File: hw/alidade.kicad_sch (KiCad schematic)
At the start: 0 parts

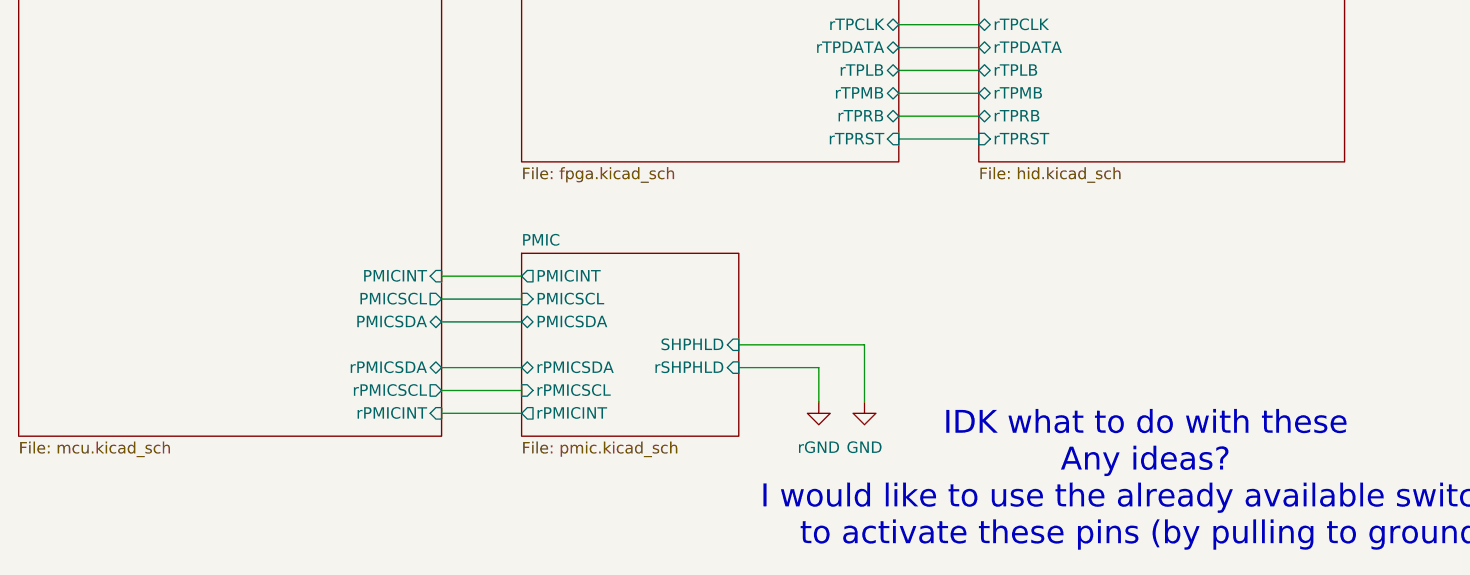
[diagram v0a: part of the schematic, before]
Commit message: Add license and organize repo
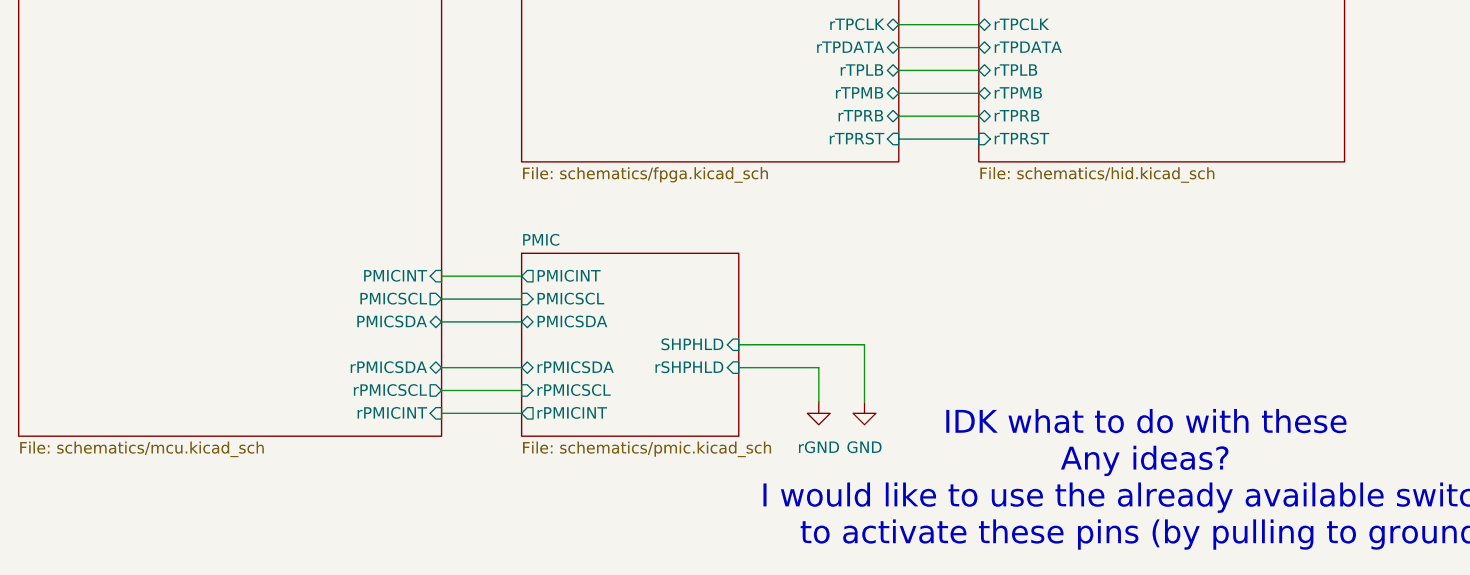
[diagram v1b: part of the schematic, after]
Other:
- sheet FPGA: file fpga.kicad_sch -> schematics/fpga.kicad_sch
- sheet HID: file hid.kicad_sch -> schematics/hid.kicad_sch
- sheet MCU: file mcu.kicad_sch -> schematics/mcu.kicad_sch
- sheet PMIC: file pmic.kicad_sch -> schematics/pmic.kicad_sch
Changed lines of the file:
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@@
 			)
 		)
-		(property "Sheetfile" "pmic.kicad_sch"
+		(property "Sheetfile" "schematics/pmic.kicad_sch"
 			(at 182.88 197.4346 0)
 			(effects
@@
 			)
 		)
-		(property "Sheetfile" "hid.kicad_sch"
+		(property "Sheetfile" "schematics/hid.kicad_sch"
 			(at 233.68 166.9546 0)
 			(effects
@@
 			)
 		)
-		(property "Sheetfile" "mcu.kicad_sch"
+		(property "Sheetfile" "schematics/mcu.kicad_sch"
 			(at 127 197.4346 0)
 			(effects
@@
 			)
 		)
-		(property "Sheetfile" "fpga.kicad_sch"
+		(property "Sheetfile" "schematics/fpga.kicad_sch"
 			(at 182.88 166.9546 0)
 			(effects

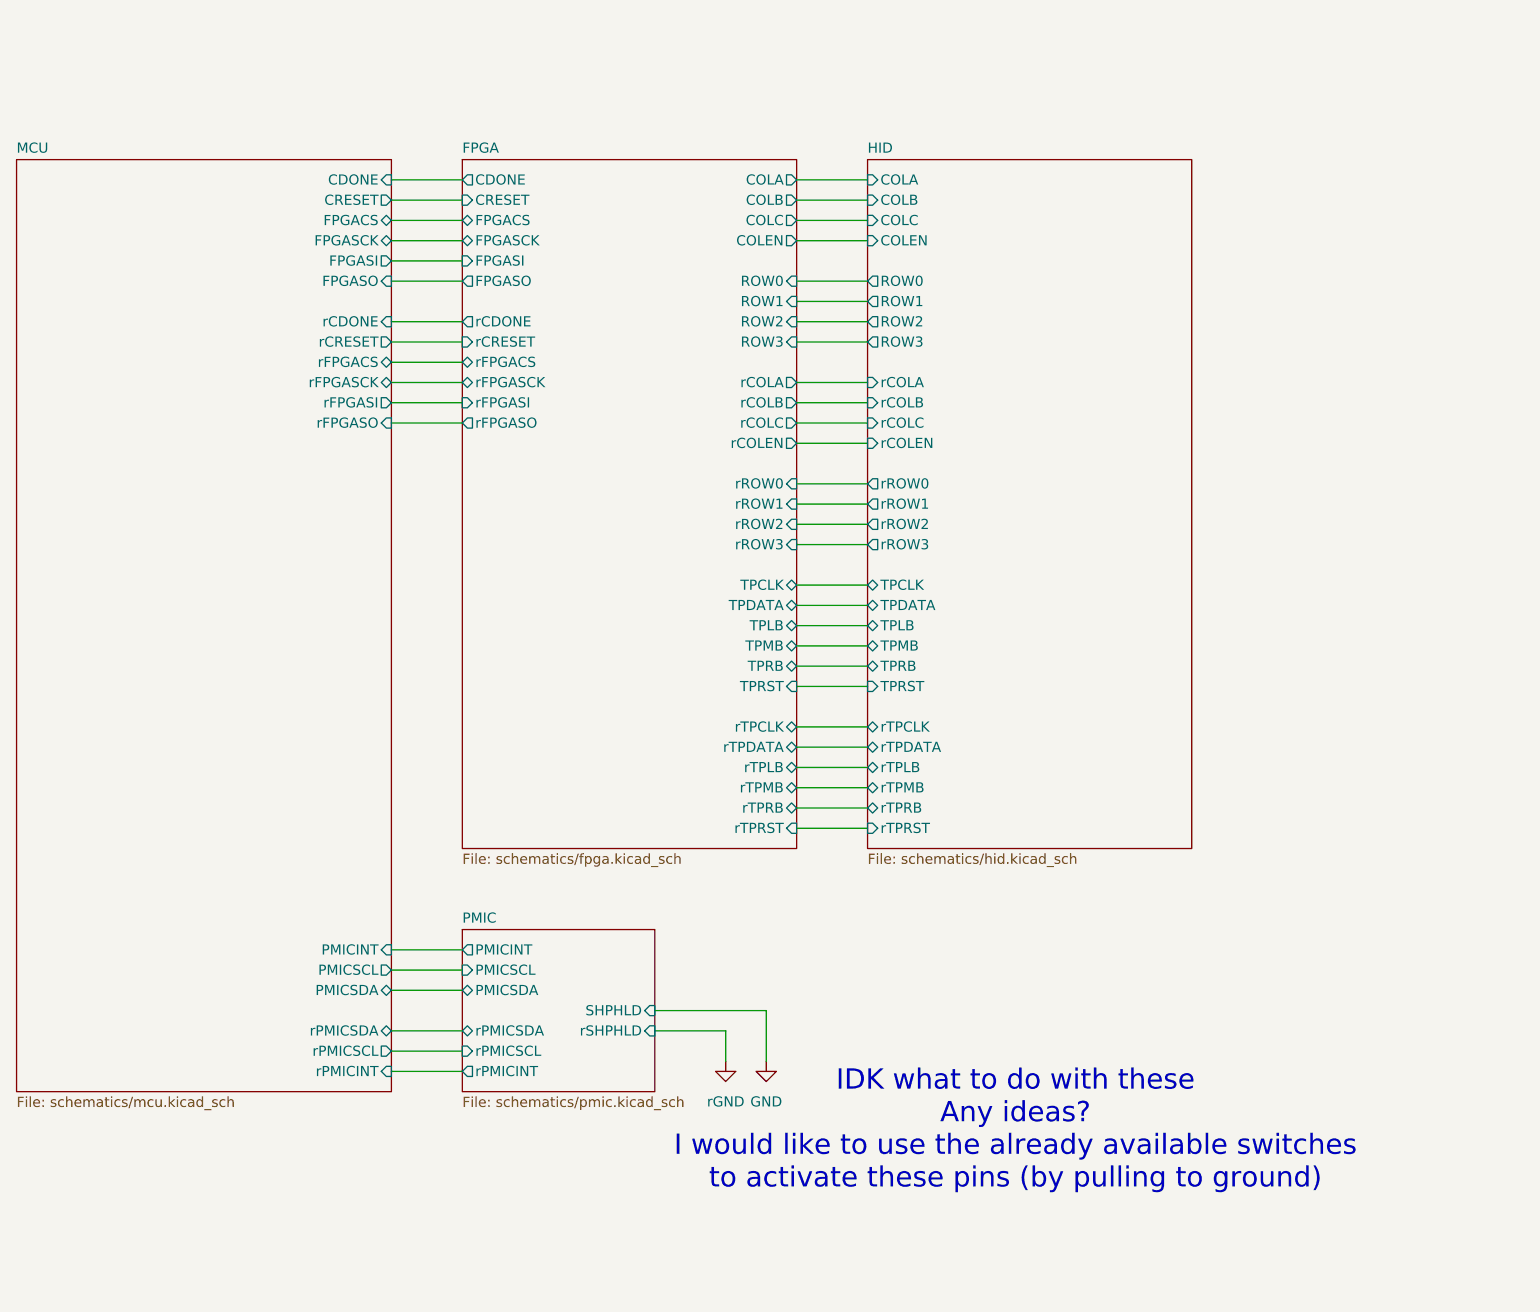
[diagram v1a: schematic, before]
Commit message: Remove SN74LVC138A as we now have enough pins on the UP
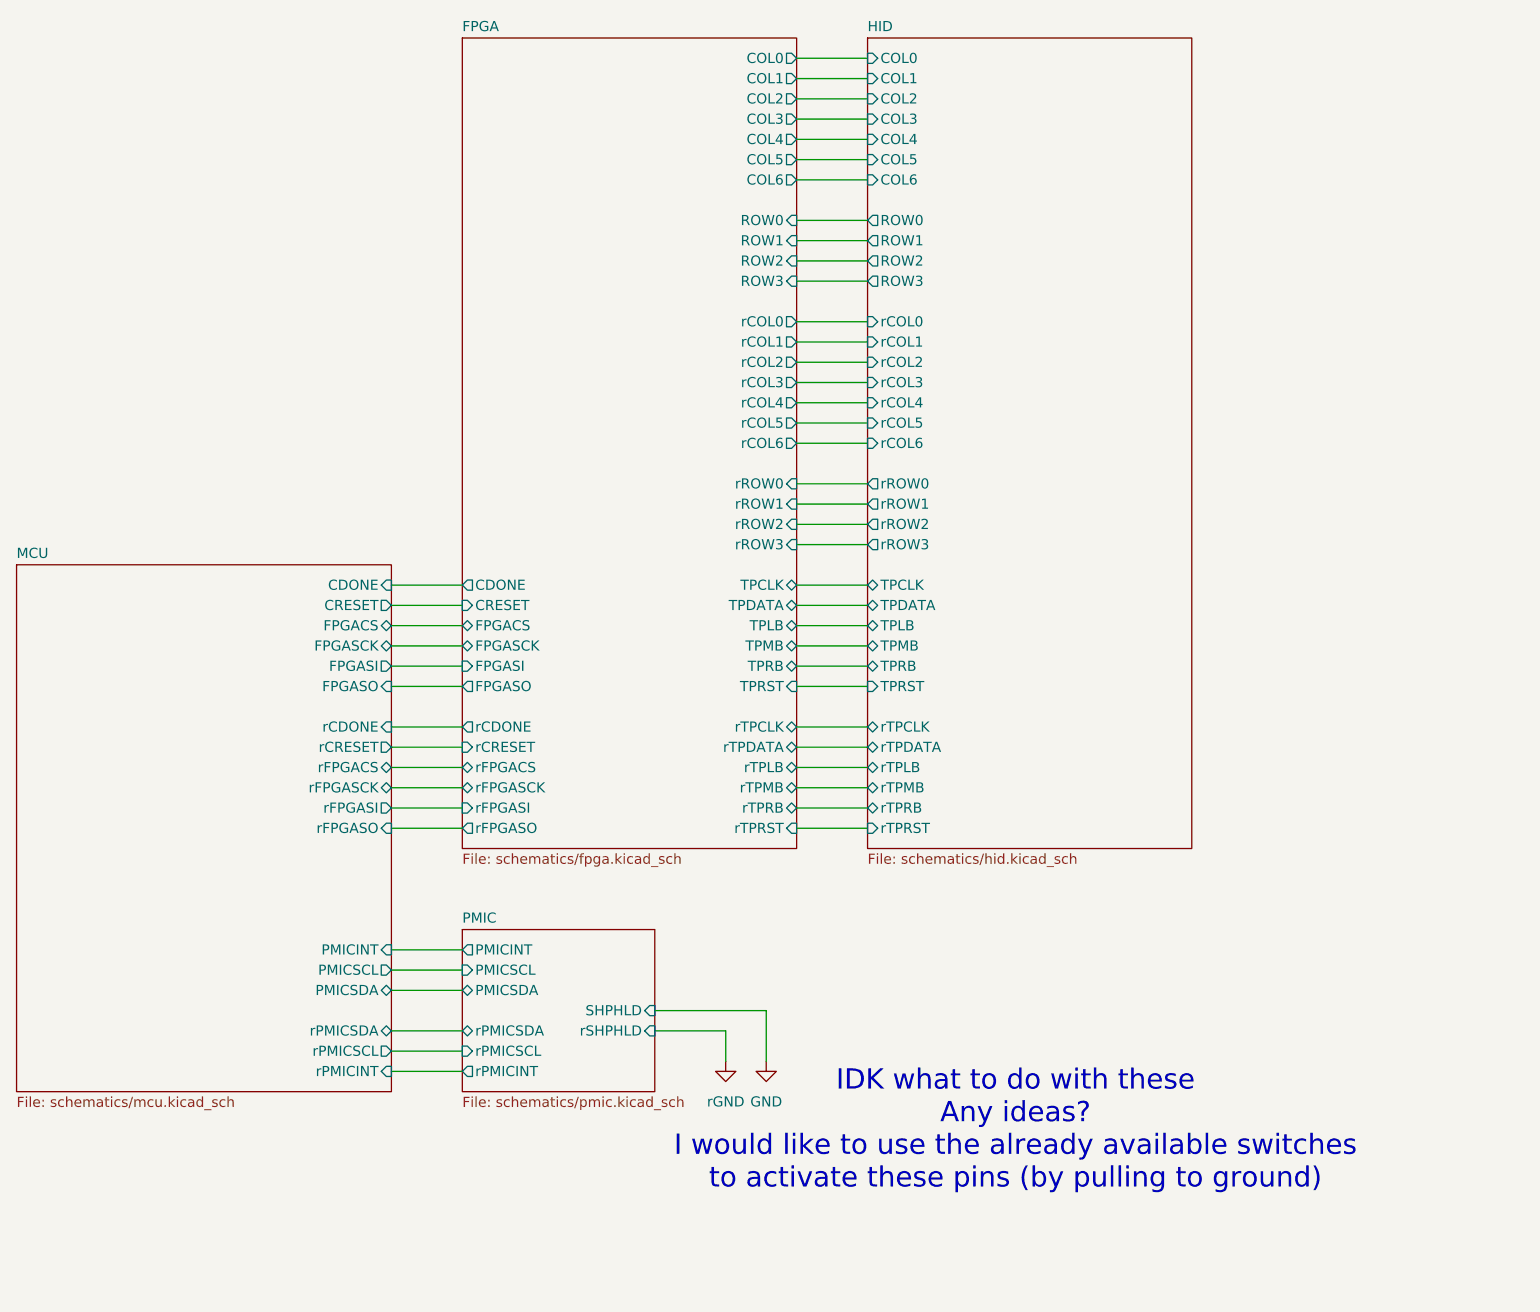
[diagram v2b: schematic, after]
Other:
- sheet FPGA ports: added COL0, COL1, COL2, COL3, COL4, COL5, COL6, rCOL0, rCOL1, rCOL2, rCOL3, rCOL4, rCOL5, rCOL6; removed COLA, COLB, COLC, COLEN, rCOLA, rCOLB, rCOLC, rCOLEN
- sheet HID ports: added COL0, COL1, COL2, COL3, COL4, COL5, COL6, rCOL0, rCOL1, rCOL2, rCOL3, rCOL4, rCOL5, rCOL6; removed COLA, COLB, COLC, COLEN, rCOLA, rCOLB, rCOLC, rCOLEN

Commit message: Remove FPGA, no longer needed
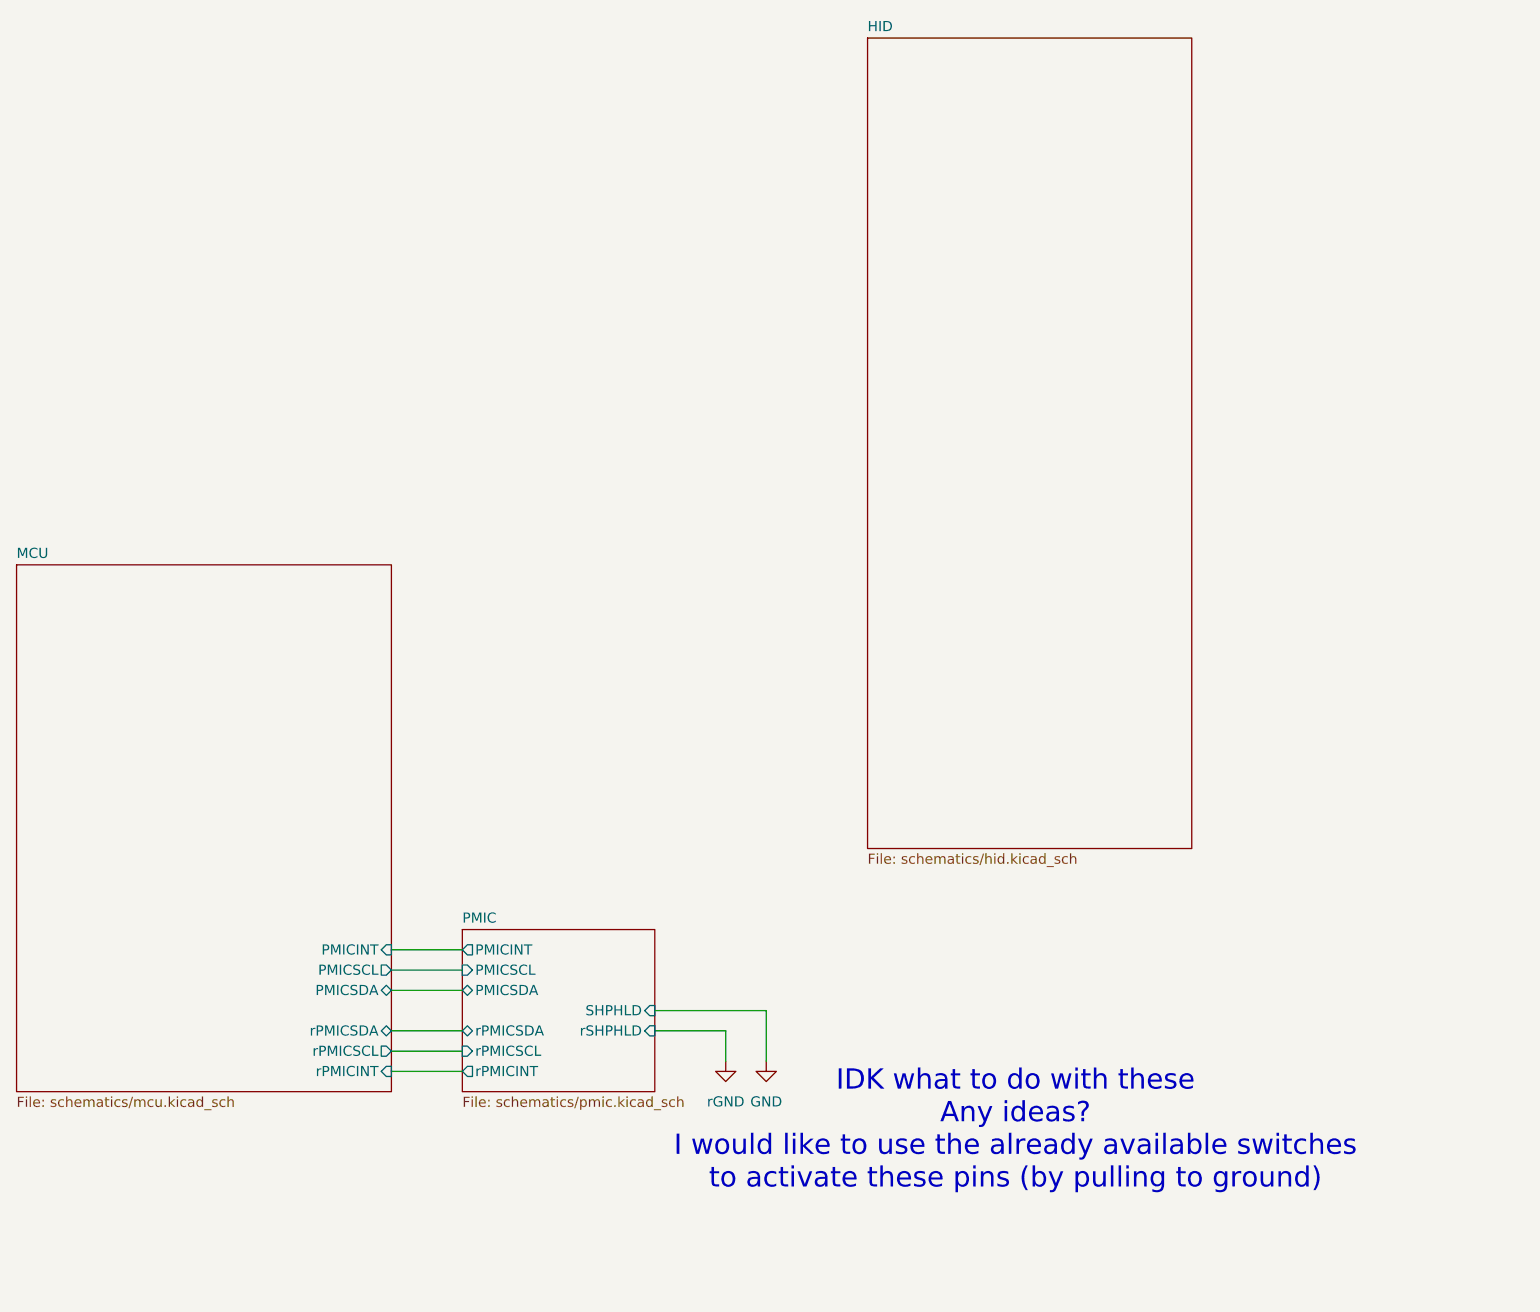
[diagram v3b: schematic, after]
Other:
- removed sheet FPGA
- sheet HID ports: added none; removed COL0, COL1, COL2, COL3, COL4, COL5, COL6, ROW0, ROW1, ROW2, ROW3, TPCLK, TPDATA, TPLB, TPMB, TPRB, TPRST, rCOL0, rCOL1, rCOL2, rCOL3, rCOL4, rCOL5, rCOL6, rROW0, rROW1, rROW2, rROW3, rTPCLK, rTPDATA, rTPLB, rTPMB, rTPRB, rTPRST
- sheet MCU ports: added none; removed CDONE, CRESET, FPGACS, FPGASCK, FPGASI, FPGASO, rCDONE, rCRESET, rFPGACS, rFPGASCK, rFPGASI, rFPGASO

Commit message: Update symbol, use ads122S for bridge measurement
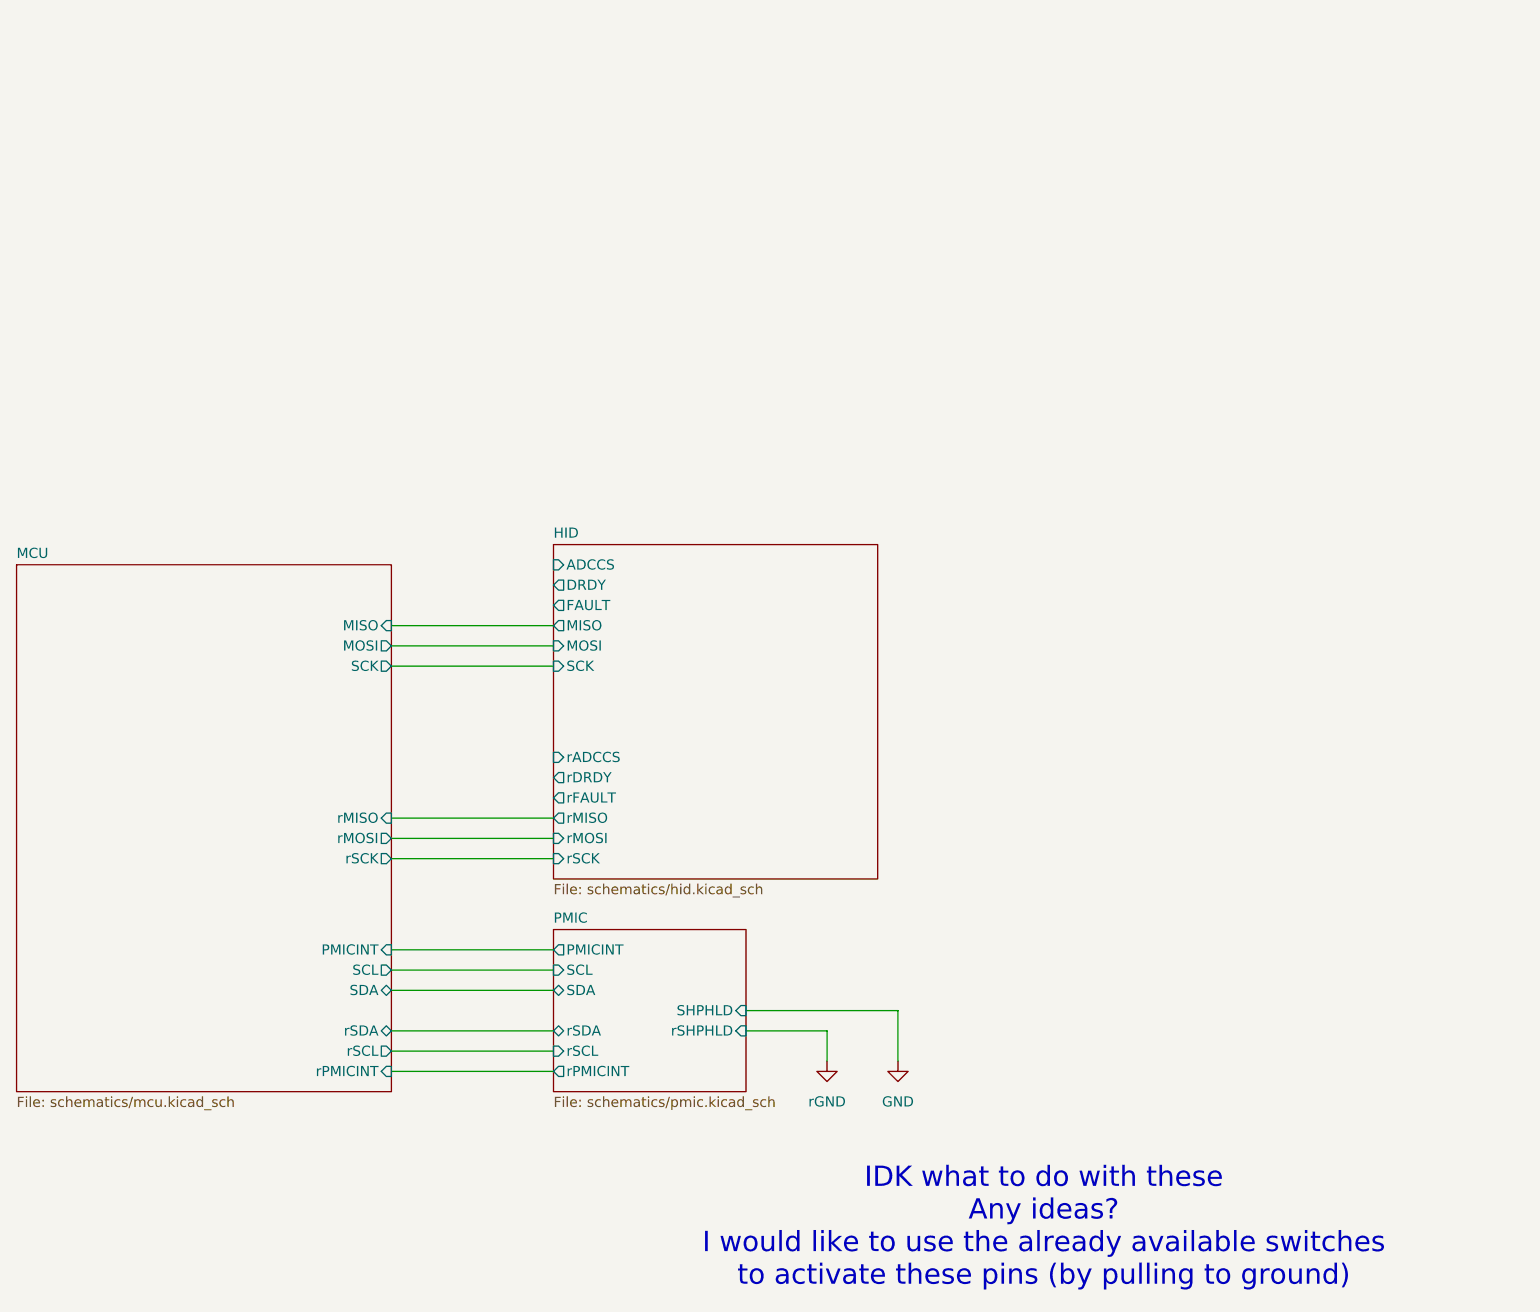
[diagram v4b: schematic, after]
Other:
- sheet HID ports: added ADCCS, DRDY, FAULT, MISO, MOSI, SCK, rADCCS, rDRDY, rFAULT, rMISO, rMOSI, rSCK; removed none
- sheet MCU ports: added MISO, MOSI, SCK, SCL, SDA, rMISO, rMOSI, rSCK, rSCL, rSDA; removed PMICSCL, PMICSDA, rPMICSCL, rPMICSDA
- sheet PMIC ports: added SCL, SDA, rSCL, rSDA; removed PMICSCL, PMICSDA, rPMICSCL, rPMICSDA
